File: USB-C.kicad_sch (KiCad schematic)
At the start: 4 parts, among them J1 USB_C_Receptacle, SW1 SW, U5 FT201XQ, U6 USB3740B-AI9

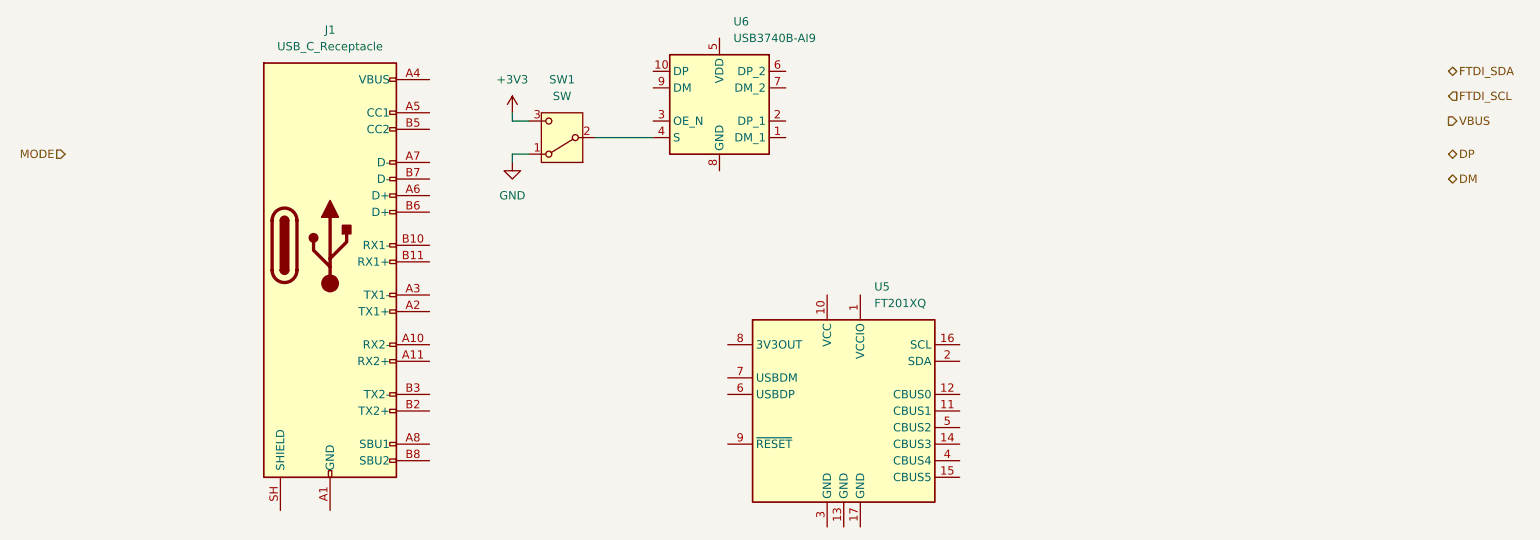
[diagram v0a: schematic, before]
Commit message: Added power schematic
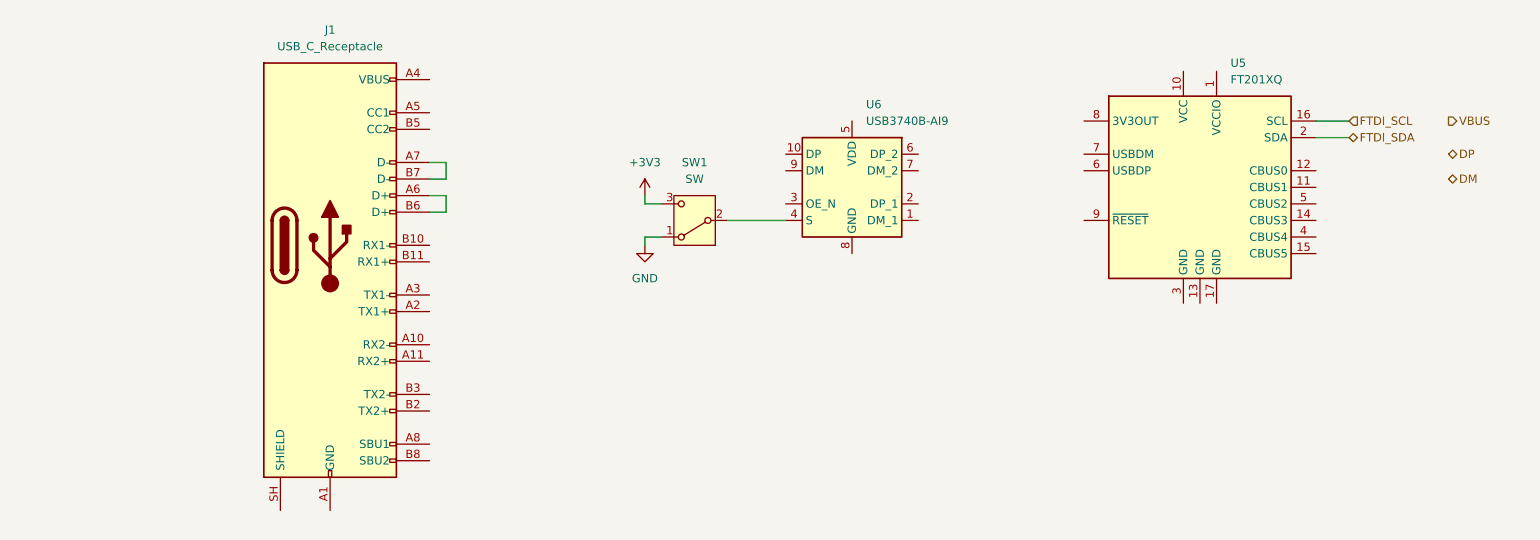
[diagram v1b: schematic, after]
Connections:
- net FTDI_SCL: now also U5.16 (SCL)
- net FTDI_SDA: now also U5.2 (SDA)
- net at J1.A6 (D+): now also J1.B6 (D+)
- net at J1.A7 (D-): now also J1.B7 (D-)
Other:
- moved on the sheet: SW1, U5, U6
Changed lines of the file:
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@@
 	(wire
 		(pts
-			(xy 107.95 91.44) (xy 110.49 91.44)
-		)
-		(stroke
-			(width 0)
-			(type default)
-		)
-	)
-	(wire
-		(pts
-			(xy 120.65 88.9) (xy 129.54 88.9)
-		)
-		(stroke
-			(width 0)
-			(type default)
-		)
-	)
-	(wire
-		(pts
-			(xy 107.95 85.09) (xy 107.95 86.36)
-		)
-		(stroke
-			(width 0)
-			(type default)
-		)
-	)
-	(wire
-		(pts
-			(xy 107.95 86.36) (xy 110.49 86.36)
-		)
-		(stroke
-			(width 0)
-			(type default)
-		)
-	)
-	(wire
-		(pts
-			(xy 107.95 92.71) (xy 107.95 91.44)
+			(xy 128.27 104.14) (xy 130.81 104.14)
+		)
+		(stroke
+			(width 0)
+			(type default)
+		)
+	)
+	(wire
+		(pts
+			(xy 140.97 101.6) (xy 149.86 101.6)
+		)
+		(stroke
+			(width 0)
+			(type default)
+		)
+	)
+	(wire
+		(pts
+			(xy 97.79 92.71) (xy 97.79 95.25)
+		)
+		(stroke
+			(width 0)
+			(type default)
+		)
+	)
+	(wire
+		(pts
+			(xy 95.25 95.25) (xy 97.79 95.25)
+		)
+		(stroke
+			(width 0)
+			(type default)
+		)
+	)
+	(wire
+		(pts
+			(xy 128.27 97.79) (xy 128.27 99.06)
+		)
+		(stroke
+			(width 0)
+			(type default)
+		)
+	)
+	(wire
+		(pts
+			(xy 97.79 97.79) (xy 97.79 100.33)
+		)
+		(stroke
+			(width 0)
+			(type default)
+		)
+	)
+	(wire
+		(pts
+			(xy 95.25 92.71) (xy 97.79 92.71)
+		)
+		(stroke
+			(width 0)
+			(type default)
+		)
+	)
+	(wire
+		(pts
+			(xy 95.25 97.79) (xy 97.79 97.79)
+		)
+		(stroke
+			(width 0)
+			(type default)
+		)
+	)
+	(wire
+		(pts
+			(xy 236.22 88.9) (xy 231.14 88.9)
+		)
+		(stroke
+			(width 0)
+			(type default)
+		)
+	)
+	(wire
+		(pts
+			(xy 128.27 99.06) (xy 130.81 99.06)
+		)
+		(stroke
+			(width 0)
+			(type default)
+		)
+	)
+	(wire
+		(pts
+			(xy 128.27 105.41) (xy 128.27 104.14)
+		)
+		(stroke
+			(width 0)
+			(type default)
+		)
+	)
+	(wire
+		(pts
+			(xy 95.25 100.33) (xy 97.79 100.33)
+		)
+		(stroke
+			(width 0)
+			(type default)
+		)
+	)
+	(wire
+		(pts
+			(xy 236.22 86.36) (xy 231.14 86.36)
 		)
 		(stroke
@@
 	(hierarchical_label "FTDI_SDA"
 		(shape bidirectional)
-		(at 251.46 78.74 0)
+		(at 236.22 88.9 0)
 		(effects
 			(font
@@
 		)
 	)
-	(hierarchical_label "MODE"
-		(shape input)
-		(at 39.37 91.44 180)
-		(effects
-			(font
-				(size 1.27 1.27)
-			)
-			(justify right)
-		)
-	)
 	(hierarchical_label "FTDI_SCL"
 		(shape input)
-		(at 251.46 82.55 0)
+		(at 236.22 86.36 0)
 		(effects
 			(font
@@
 	(symbol
 		(lib_id "Interface_USB:FT201XQ")
-		(at 158.75 130.81 0)
+		(at 213.36 96.52 0)
 		(unit 1)
 		(body_style 1)
@@
 		(fields_autoplaced yes)
 		(property "Reference" "U5"
-			(at 163.4333 111.76 0)
+			(at 218.0433 77.47 0)
 			(show_name no)
 			(do_not_autoplace no)
@@
 		)
 		(property "Value" "FT201XQ"
-			(at 163.4333 114.3 0)
+			(at 218.0433 80.01 0)
 			(show_name no)
 			(do_not_autoplace no)
@@
 		)
 		(property "Footprint" "Package_DFN_QFN:QFN-16-1EP_4x4mm_P0.65mm_EP2.1x2.1mm"
-			(at 193.04 146.05 0)
+			(at 247.65 111.76 0)
 			(hide yes)
 			(show_name no)
@@
 		)
 		(property "Datasheet" "https://www.ftdichip.com/Support/Documents/DataSheets/ICs/DS_FT201X.pdf"
-			(at 158.75 130.81 0)
+			(at 213.36 96.52 0)
 			(hide yes)
 			(show_name no)
@@
 		)
 		(property "Description" "Full Speed USB to I2C Bridge, QFN-10"
-			(at 158.75 130.81 0)
+			(at 213.36 96.52 0)
 			(hide yes)
 			(show_name no)
@@
 	(symbol
 		(lib_id "power:GND")
-		(at 107.95 92.71 0)
+		(at 128.27 105.41 0)
 		(unit 1)
 		(body_style 1)
@@
 		(fields_autoplaced yes)
 		(property "Reference" "#PWR05"
-			(at 107.95 99.06 0)
+			(at 128.27 111.76 0)
 			(hide yes)
 			(show_name no)
@@
 		)
 		(property "Value" "GND"
-			(at 107.95 97.79 0)
+			(at 128.27 110.49 0)
 			(show_name no)
 			(do_not_autoplace no)
@@
 		)
 		(property "Footprint" ""
-			(at 107.95 92.71 0)
+			(at 128.27 105.41 0)
 			(hide yes)
 			(show_name no)
@@
 		)
 		(property "Datasheet" ""
-			(at 107.95 92.71 0)
+			(at 128.27 105.41 0)
 			(hide yes)
 			(show_name no)
@@
 		)
 		(property "Description" "Power symbol creates a global label with name \"GND\" , ground"
-			(at 107.95 92.71 0)
+			(at 128.27 105.41 0)
 			(hide yes)
 			(show_name no)
@@
 	(symbol
 		(lib_id "Interface_USB:USB3740B-AI9")
-		(at 139.7 83.82 0)
+		(at 160.02 96.52 0)
 		(unit 1)
 		(body_style 1)
@@
 		(fields_autoplaced yes)
 		(property "Reference" "U6"
-			(at 141.8433 71.12 0)
+			(at 162.1633 83.82 0)
 			(show_name no)
 			(do_not_autoplace no)
@@
 		)
 		(property "Value" "USB3740B-AI9"
-			(at 141.8433 73.66 0)
+			(at 162.1633 86.36 0)
 			(show_name no)
 			(do_not_autoplace no)
@@
 		)
 		(property "Footprint" "Package_DFN_QFN:UQFN-10_1.6x2.1mm_P0.5mm"
-			(at 170.18 92.71 0)
+			(at 190.5 105.41 0)
 			(hide yes)
 			(show_name no)
@@
 		)
 		(property "Datasheet" "http://ww1.microchip.com/downloads/en/DeviceDoc/00001725D.pdf"
-			(at 139.7 86.36 0)
+			(at 160.02 99.06 0)
 			(hide yes)
 			(show_name no)
@@
 		)
 		(property "Description" "USB 2.0 Switch with ESD Protection, UQFN-10 Pitch 0.5mm"
-			(at 139.7 83.82 0)
+			(at 160.02 96.52 0)
 			(hide yes)
 			(show_name no)
@@
 	(symbol
 		(lib_id "power:+3V3")
-		(at 107.95 85.09 0)
+		(at 128.27 97.79 0)
 		(unit 1)
 		(body_style 1)
@@
 		(fields_autoplaced yes)
 		(property "Reference" "#PWR014"
-			(at 107.95 88.9 0)
+			(at 128.27 101.6 0)
 			(hide yes)
 			(show_name no)
@@
 		)
 		(property "Value" "+3V3"
-			(at 107.95 80.01 0)
+			(at 128.27 92.71 0)
 			(show_name no)
 			(do_not_autoplace no)
@@
 		)
 		(property "Footprint" ""
-			(at 107.95 85.09 0)
+			(at 128.27 97.79 0)
 			(hide yes)
 			(show_name no)
@@
 		)
 		(property "Datasheet" ""
-			(at 107.95 85.09 0)
+			(at 128.27 97.79 0)
 			(hide yes)
 			(show_name no)
@@
 		)
 		(property "Description" "Power symbol creates a global label with name \"+3V3\""
-			(at 107.95 85.09 0)
+			(at 128.27 97.79 0)
 			(hide yes)
 			(show_name no)
@@
 	(symbol
 		(lib_id "Switch:SW_SPDT")
-		(at 115.57 88.9 180)
+		(at 135.89 101.6 180)
 		(unit 1)
 		(body_style 1)
@@
 		(fields_autoplaced yes)
 		(property "Reference" "SW1"
-			(at 115.57 80.01 0)
+			(at 135.89 92.71 0)
 			(show_name no)
 			(do_not_autoplace no)
@@
 		)
 		(property "Value" "SW"
-			(at 115.57 82.55 0)
+			(at 135.89 95.25 0)
 			(show_name no)
 			(do_not_autoplace no)
@@
 		)
 		(property "Footprint" ""
-			(at 115.57 88.9 0)
+			(at 135.89 101.6 0)
 			(hide yes)
 			(show_name no)
@@
 		)
 		(property "Datasheet" ""
-			(at 115.57 81.28 0)
+			(at 135.89 93.98 0)
 			(hide yes)
 			(show_name no)
@@
 		)
 		(property "Description" "Switch, single pole double throw"
-			(at 115.57 88.9 0)
-			(hide yes)
-			(show_name no)
+			(at 135.89 101.6 0)
+			(hide yes)
+			(show_name no)

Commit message: Added todos
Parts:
- removed J1: USB_C_Receptacle, Connector_USB:USB_C_Receptacle_Amphenol_12401548E4-2A_CircularHoles, symbol Connector:USB_C_Receptacle
- added J3: USB_C_Receptacle_USB2.0_16P, Connector_USB:USB_C_Receptacle_GCT_USB4110, symbol Connector:USB_C_Receptacle_USB2.0_16P
- added R12, R13: 5k1, Resistor_SMD:R_0603_1608Metric, symbol Device:R
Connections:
- net +3V3: now also U5.1 (VCCIO), U5.9 (~{RESET})
- net DM: now also U6.1 (DM_1), U6.9 (DM), J3.A7 (D-), J3.B7 (D-)
- net DP: now also U6.10 (DP), U6.2 (DP_1), J3.A6 (D+), J3.B6 (D+)
- net GND: now also U5.13 (GND), U5.17 (GND), U5.3 (GND), U6.3 (OE_N), U6.8 (GND), J3.A1 (GND), J3.A12 (GND), J3.A8 (SBU1), J3.B1 (GND), J3.B12 (GND), J3.B8 (SBU2), J3.SH (SHIELD), R12.2, R13.2
- net VBUS: now also J3.A4 (VBUS), J3.A9 (VBUS), J3.B4 (VBUS), J3.B9 (VBUS)
- net +5V: now reaches U5.10 (VCC)
- net +5V: now also U6.5 (VDD)
- net FT_PWREN: now reaches U5.14 (CBUS3)
- net FT_KEEP_AWAKE: now reaches U5.15 (CBUS5)
- net DP_2: now reaches U5.6 (USBDP)
- net DP_2: now also U6.6 (DP_2)
- net DM_2: now reaches U5.7 (USBDM)
- net DM_2: now also U6.7 (DM_2)
- new net: J3.B5 (CC2), R12.1
- new net: J3.A5 (CC1), R13.1
- no-connect marks 0 -> 5
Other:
- note added: "Connector"
- note added: "FT201X"
- note added: "MUX"
- moved on the sheet: SW1, U5, U6

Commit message: Started PCB
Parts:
- added C14, C17: 100n, Capacitor_SMD:C_0402_1005Metric, symbol Device:C
- added C15, C16: 1u, Capacitor_SMD:C_0603_1608Metric, symbol Device:C
- added R14: 5k1, Resistor_SMD:R_0603_1608Metric, symbol Device:R
- added R15: 10k, Resistor_SMD:R_0603_1608Metric, symbol Device:R
- added R16, R17: 27, Resistor_SMD:R_0603_1608Metric, symbol Device:R
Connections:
- net +3V3: now also C16.1
- net +5V: now also C14.1, C15.1, C17.1
- net DM_2: now also R16.2; no longer U5.7 (USBDM)
- net DP_2: now also R17.2; no longer U5.6 (USBDP)
- net GND: now also C14.2, C15.2, C16.2, C17.2, R15.2
- net VBUS: now also R14.1
- net at U5.4 (CBUS4): now also R14.2, R15.1
- new net: R17.1, U5.6 (USBDP)
- new net: R16.1, U5.7 (USBDM)
- no-connect marks 5 -> 4
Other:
- moved on the sheet: SW1, U5, U6
